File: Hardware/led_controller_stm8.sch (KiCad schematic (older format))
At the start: 11 parts, among them J1 WS_LED, J2 PROGRAMMING, J3 EXT_BTN, SW1 SW_Push, U1 STM8S103F3

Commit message: add pcb
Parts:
- removed C3: 1nF, Capacitor_SMD:C_0805_2012Metric_Pad1.15x1.40mm_HandSolder, symbol Device:C
- removed J3: EXT_BTN, Connector_JST:JST_PH_B2B-PH-K_1x02_P2.00mm_Vertical, symbol Connector_Generic:Conn_01x02
- added D1: BAV99, Package_TO_SOT_SMD:SOT-23, symbol Diode:BAV99
- added Q1, Q2: IRLML6401, Package_TO_SOT_SMD:SOT-23, symbol Transistor_FET:IRLML6401
- added Q3: 2N7002, Package_TO_SOT_SMD:SOT-23, symbol Transistor_FET:2N7002
- added Q4: MMBT3904, Package_TO_SOT_SMD:SOT-23, symbol Transistor_BJT:MMBT3904
- added R2: 15k, Resistor_SMD:R_0805_2012Metric_Pad1.15x1.40mm_HandSolder, symbol Device:R
- added R3, R4, R6: 150k, Resistor_SMD:R_0805_2012Metric_Pad1.15x1.40mm_HandSolder, symbol Device:R
- added R5: 100, Resistor_SMD:R_0805_2012Metric_Pad1.15x1.40mm_HandSolder, symbol Device:R
- added R7: 470, Resistor_SMD:R_0805_2012Metric_Pad1.15x1.40mm_HandSolder, symbol Device:R
- J2: renamed from J1; footprint Connector_JST:JST_PH_B3B-PH-K_1x03_P2.00mm_Vertical -> Connector_JST:JST_XH_B3B-XH-A_1x03_P2.50mm_Vertical
- R1: value 12k -> 150k
- renumbered C4 to C3, J2 to J1
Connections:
- net +BATT: now also J2.1 (Pin_1), D1.1 (K), Q2.3 (D), R2.1; no longer BT1.1 (+), J2.2 (Pin_2), R1.1
- net BTN: now also U1.12 ([ADC_ETR]_I2C_SCL/PB4(T)), Q4.3 (C), R2.2; no longer R1.2, SW1.1, U1.10 ([SPI_NSS]_TIM2_CH3/HS_PA3)
- net GND: now also J2.3 (Pin_3), SW1.1, R4.2, R5.2, R6.2; no longer J2.1 (Pin_1), SW1.2
- net WS_LED: now also R7.2; no longer J2.3 (Pin_3)
- net PWR_EN: now reaches U1.1 (UART1_CK/TIM2_CH1/CH1/BEEP/HS_PD4)
- net PWR_EN: now also Q3.1 (G), R3.1
- net BAT_ADC_2: now reaches U1.19 ([TIM2_CH3]_AIN3/HS_PD2)
- net BAT_ADC_2: now also D1.2 (A), R6.1
- net BAT_ADC_1: now reaches U1.20 (ADC_ETR/TIM2_CH2/AIN4/HS_PD3)
- net BAT_ADC_1: now also D1.3 (K)
- new net: J2.2 (Pin_2), R7.1
- new net: BT1.1 (+), Q1.3 (D)
- new net: Q1.1 (G), R4.1
- new net: Q1.2 (S), Q2.2 (S), R1.1
- new net: Q2.1 (G), Q3.3 (D), R1.2, SW1.2
- new net: Q3.2 (S), Q4.1 (B), R3.2
- new net: Q4.2 (E), R5.1
- no-connect marks 12 -> 9
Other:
- moved on the sheet: BT1, C1, C2, C3, J1, J2, U1

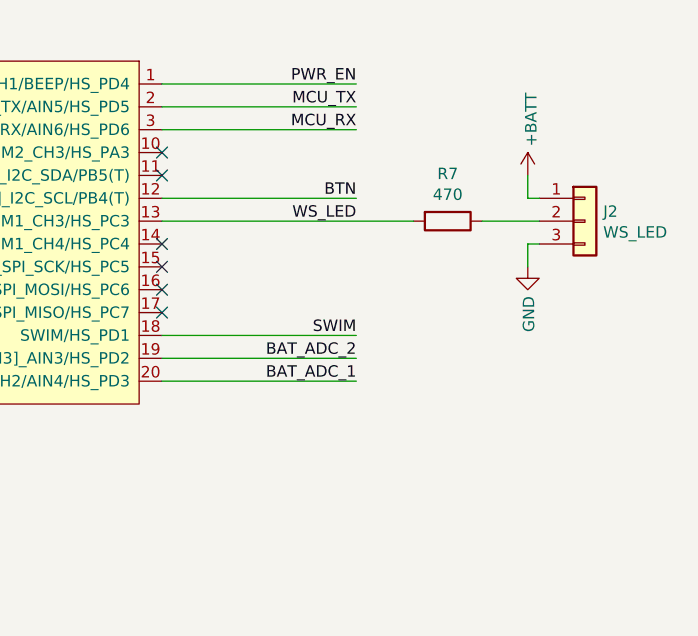
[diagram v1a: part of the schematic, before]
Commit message: add second horizontal led connector
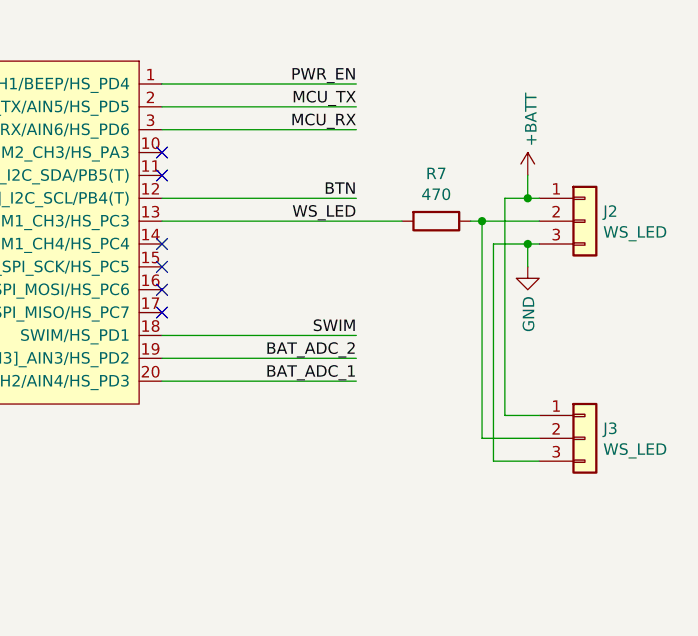
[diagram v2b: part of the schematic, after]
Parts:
- added J3: WS_LED, Connector_JST:JST_XH_B3B-XH-A_1x03_P2.50mm_Vertical, symbol Connector_Generic:Conn_01x03
- J2: footprint Connector_JST:JST_XH_B3B-XH-A_1x03_P2.50mm_Vertical -> Connector_JST:JST_XH_S3B-XH-A-1_1x03_P2.50mm_Horizontal
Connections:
- net +BATT: now also J3.1 (Pin_1)
- net GND: now also J3.3 (Pin_3)
- net at J2.2 (Pin_2), R7.1: now also J3.2 (Pin_2)
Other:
- moved on the sheet: R7
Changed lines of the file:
@@
 F 0 "J2" H 10530 2742 50  0000 L CNN
 F 1 "WS_LED" H 10530 2651 50  0000 L CNN
-F 2 "Connector_JST:JST_XH_B3B-XH-A_1x03_P2.50mm_Vertical" H 10450 2700 50  0001 C CNN
+F 2 "Connector_JST:JST_XH_S3B-XH-A-1_1x03_P2.50mm_Horizontal" H 10450 2700 50  0001 C CNN
 F 3 "~" H 10450 2700 50  0001 C CNN
 	1    10450 2700
@@
 L Device:R R7
 U 1 1 61585399
-P 9850 2700
-F 0 "R7" V 9643 2700 50  0000 C CNN
-F 1 "470" V 9734 2700 50  0000 C CNN
-F 2 "Resistor_SMD:R_0805_2012Metric_Pad1.15x1.40mm_HandSolder" V 9780 2700 50  0001 C CNN
-F 3 "~" H 9850 2700 50  0001 C CNN
-	1    9850 2700
+P 9800 2700
+F 0 "R7" V 9593 2700 50  0000 C CNN
+F 1 "470" V 9684 2700 50  0000 C CNN
+F 2 "Resistor_SMD:R_0805_2012Metric_Pad1.15x1.40mm_HandSolder" V 9730 2700 50  0001 C CNN
+F 3 "~" H 9800 2700 50  0001 C CNN
+	1    9800 2700
 	0    1    1    0
 $EndComp
-Wire Wire Line
-	9700 2700 8600 2700
+$Comp
+L Connector_Generic:Conn_01x03 J3
+U 1 1 615A65A3
+P 10450 3650
+F 0 "J3" H 10530 3692 50  0000 L CNN
+F 1 "WS_LED" H 10530 3601 50  0000 L CNN
+F 2 "Connector_JST:JST_XH_B3B-XH-A_1x03_P2.50mm_Vertical" H 10450 3650 50  0001 C CNN
+F 3 "~" H 10450 3650 50  0001 C CNN
+	1    10450 3650
+	1    0    0    -1
+$EndComp
+Wire Wire Line
+	10200 2600 10100 2600
+Wire Wire Line
+	10100 2600 10100 3550
+Wire Wire Line
+	10100 3550 10250 3550
+Connection ~ 10200 2600
+Wire Wire Line
+	10200 2800 10050 2800
+Wire Wire Line
+	10050 2800 10050 3750
+Wire Wire Line
+	10050 3750 10250 3750
+Connection ~ 10200 2800
+Wire Wire Line
+	9650 2700 8600 2700
+Wire Wire Line
+	9950 2700 10000 2700
+Wire Wire Line
+	10000 2700 10000 3650
+Wire Wire Line
+	10000 3650 10250 3650
+Connection ~ 10000 2700
 Wire Wire Line
 	10000 2700 10250 2700
